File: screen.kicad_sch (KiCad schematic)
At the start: 12 parts, among them U4 3寸液晶屏TFT 全新无定义资料, U9 STI9287C

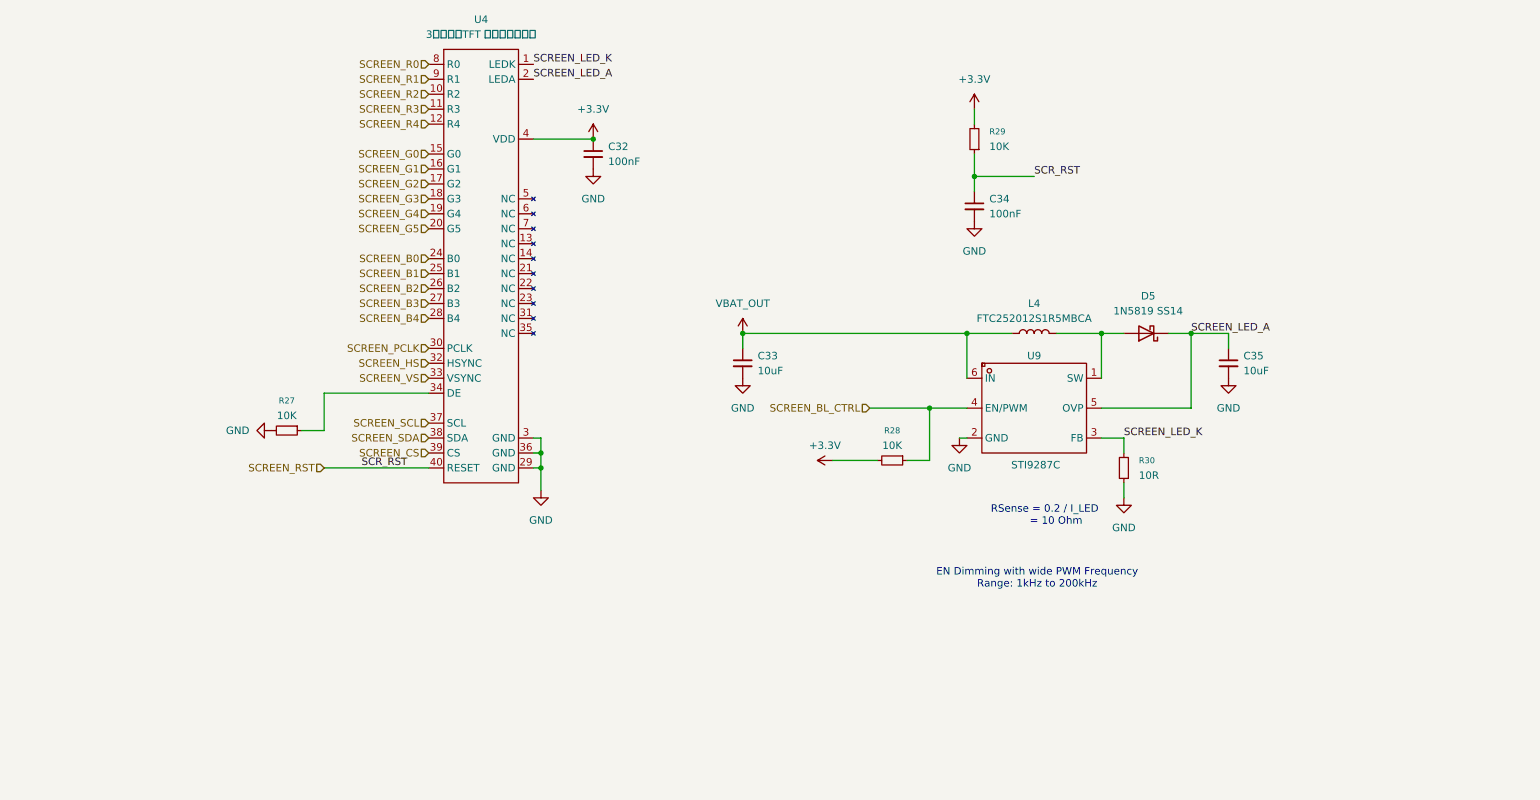
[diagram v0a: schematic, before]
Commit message: V0.3.1 bugfix
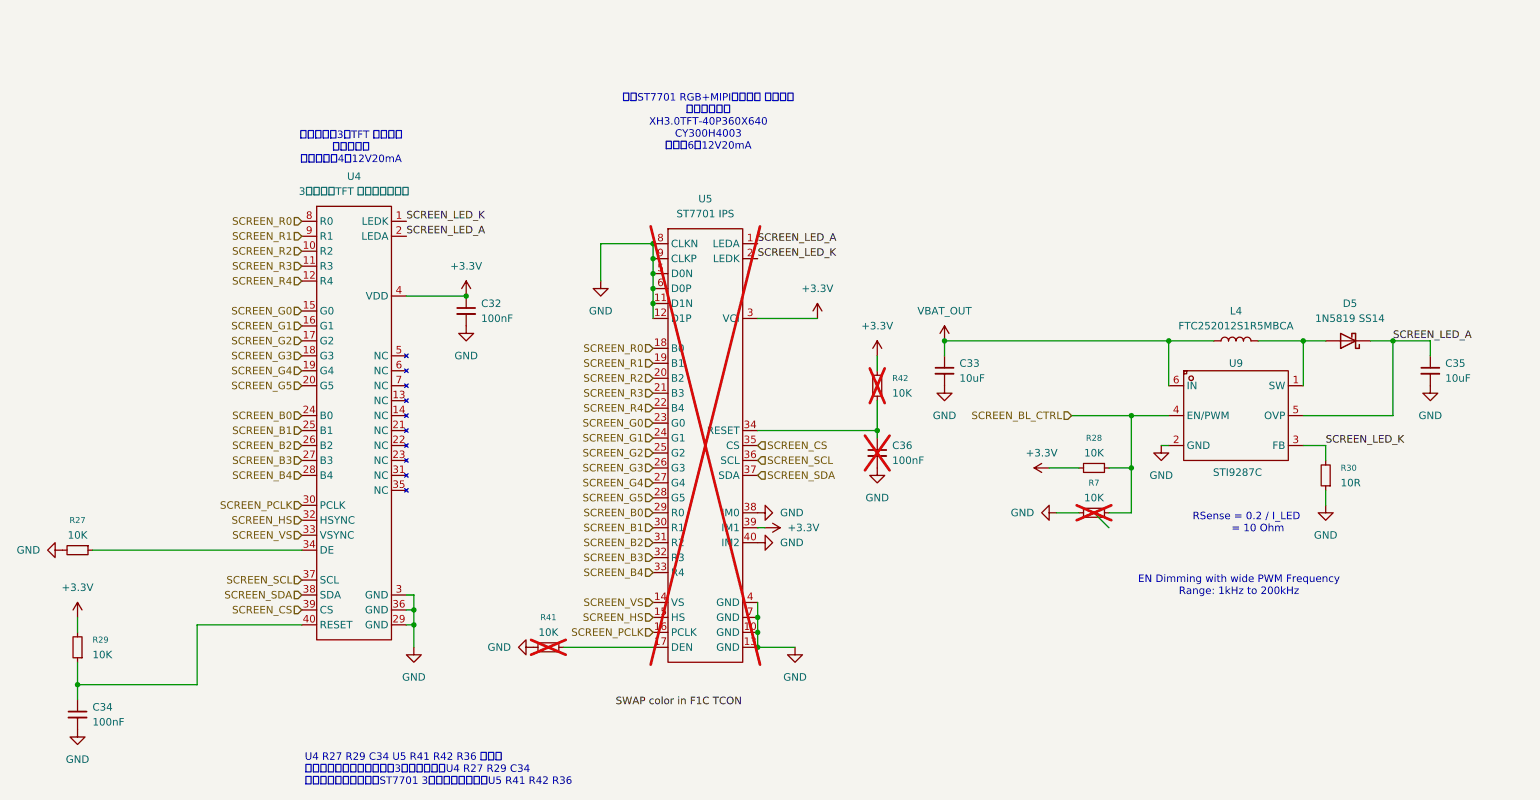
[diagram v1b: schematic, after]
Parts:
- added C36: 100nF, Capacitor_SMD:C_0603_1608Metric, symbol Device:C_Small
- added R41, R42, R7: 10K, Resistor_SMD:R_0603_1608Metric, symbol Device:R_Small
- added U5: ST7701 IPS, Connector_FFC-FPC:Hirose_FH12-40S-0.5SH_1x40-1MP_P0.50mm_Horizontal, symbol shirogane:CY300H4003
- C34, R27, R29, U4: 特殊说明 (none) -> 3元TFT贴装
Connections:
- net +3.3V: now also R42.2, U5.3 (VCI), U5.39 (IM1)
- net GND: now also C36.2, R41.2, R7.2, U5.10 (GND), U5.11 (D1N), U5.12 (D1P), U5.13 (GND), U5.38 (IM0), U5.4 (GND), U5.40 (IM2), U5.5 (D0N), U5.6 (D0P), U5.7 (GND), U5.8 (CLKN), U5.9 (CLKP)
- net SCREEN_B0: now also U5.29 (R0)
- net SCREEN_B1: now also U5.30 (R1)
- net SCREEN_B2: now also U5.31 (R2)
- net SCREEN_B3: now also U5.32 (R3)
- net SCREEN_B4: now also U5.33 (R4)
- net SCREEN_BL_CTRL: now also R7.1
- net SCREEN_CS: now also U5.35 (CS)
- net SCREEN_G0: now also U5.23 (G0)
- net SCREEN_G1: now also U5.24 (G1)
- net SCREEN_G2: now also U5.25 (G2)
- net SCREEN_G3: now also U5.26 (G3)
- net SCREEN_G4: now also U5.27 (G4)
- net SCREEN_G5: now also U5.28 (G5)
- net SCREEN_HS: now also U5.15 (HS)
- net SCREEN_LED_A: now also U5.1 (LEDA)
- net SCREEN_LED_K: now also U5.2 (LEDK)
- net SCREEN_PCLK: now also U5.16 (PCLK)
- net SCREEN_R0: now also U5.18 (B0)
- net SCREEN_R1: now also U5.19 (B1)
- net SCREEN_R2: now also U5.20 (B2)
- net SCREEN_R3: now also U5.21 (B3)
- net SCREEN_R4: now also U5.22 (B4)
- net SCREEN_SCL: now also U5.36 (SCL)
- net SCREEN_SDA: now also U5.37 (SDA)
- net SCREEN_VS: now also U5.14 (VS)
- net SCREEN_RST: no longer names the net of C34.1, R29.1, U4.40 (RESET)
- new net: R41.1, U5.17 (DEN)
- new net: C36.1, R42.1, U5.34 (RESET)
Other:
- note added: "U4 R27 R29 C34 U5 R41 R42 R36 说明： 若购买的屏幕是老王电子的3元屏，只贴装U4 R27 R29 C34 若购买的屏幕是通用的ST7701 3寸钢壳屏，只贴装U5 R41 R42 R36"
- note added: "老王电子的3元TFT 下接！！ （已断货） 此款背光为4串12V20mA"
- note added: "通用ST7701 RGB+MIPI屏幕接口 上接！！ 已测试型号： XH3.0TFT-40P360X640 CY300H4003 背光：6串12V20mA"
- moved on the sheet: C32, C33, C34, C35, D5, L4, R27, R28, R29, R30, U4, U9

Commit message: V0.5
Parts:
- C35: value 10uF -> 1uF
- D5: value 1N5819 SS14 -> 1N5819WS
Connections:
- net GND: now also U4.MP, U5.MP
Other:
- note added: "50V耐压！"
- note added: "SWAP color in F1C TCON"
- note added: "U4 R27 R29 C34 U5 R41 R42 R36 说明： 若购买的屏幕是老王电子的3元屏，只贴装U4 R27 R29 C34 若购买的屏幕是通用的ST7701 3寸钢壳屏，只贴装U5 R41 R42 C36"
- note removed: "U4 R27 R29 C34 U5 R41 R42 R36 说明： 若购买的屏幕是老王电子的3元屏，只贴装U4 R27 R29 C34 若购买的屏幕是通用的ST7701 3寸钢壳屏，只贴装U5 R41 R42 R36"
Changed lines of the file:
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@@
 		(comment 1 "V0.3 添加屏幕兼容接口，添加SD卡槽，优化布线")
 		(comment 2 "V0.3.1 BUG修复")
+		(comment 3 "土豆、星语Studio、爱莉希雅、所有复刻群友的支持！")
+		(comment 4 "V0.3.2 生产优化。特别感谢：（不分先后）和光、薄云、烟雨、WXNA、")
 	)
 	(text "RSense = 0.2 / I_LED \n       = 10 Ohm"
@@
 		)
 	)
-	(text "U4 R27 R29 C34 U5 R41 R42 R36 说明：\n若购买的屏幕是老王电子的3元屏，只贴装U4 R27 R29 C34\n若购买的屏幕是通用的ST7701 3寸钢壳屏，只贴装U5 R41 R42 R36"
+	(text "50V耐压！"
+		(exclude_from_sim no)
+		(at 269.24 102.616 0)
+		(effects
+			(font
+				(size 1.27 1.27)
+			)
+		)
+	)
+	(text "SWAP color in F1C TCON"
+		(exclude_from_sim no)
+		(at 135.636 159.004 0)
+		(effects
+			(font
+				(size 1.27 1.27)
+			)
+		)
+	)
+	(text "U4 R27 R29 C34 U5 R41 R42 R36 说明：\n若购买的屏幕是老王电子的3元屏，只贴装U4 R27 R29 C34\n若购买的屏幕是通用的ST7701 3寸钢壳屏，只贴装U5 R41 R42 C36"
 		(exclude_from_sim no)
 		(at 66.548 170.688 0)
@@
 	)
 	(junction
+		(at 143.51 142.24)
+		(diameter 0)
+		(color 0 0 0 0)
+	)
+	(junction
 		(at 125.73 86.36)
 		(diameter 0)
@@
 	)
 	(junction
+		(at 85.09 140.97)
+		(diameter 0)
+		(color 0 0 0 0)
+	)
+	(junction
 		(at 125.73 83.82)
 		(diameter 0)
@@
 		(color 0 0 0 0)
 	)
-	(bus_entry
-		(at 200.66 127)
-		(size 2.54 2.54)
-		(stroke
-			(width 0)
-			(type default)
-		)
-	)
 	(wire
 		(pts
@@
 	(wire
 		(pts
+			(xy 85.09 138.43) (xy 85.09 140.97)
+		)
+		(stroke
+			(width 0)
+			(type default)
+		)
+	)
+	(wire
+		(pts
 			(xy 116.84 81.28) (xy 125.73 81.28)
 		)
@@
 	(wire
 		(pts
+			(xy 143.51 139.7) (xy 143.51 142.24)
+		)
+		(stroke
+			(width 0)
+			(type default)
+		)
+	)
+	(wire
+		(pts
 			(xy 207.01 127) (xy 207.01 119.38)
 		)
@@
 		(pts
 			(xy 30.48 133.35) (xy 66.04 133.35)
+		)
+		(stroke
+			(width 0)
+			(type default)
+		)
+	)
+	(wire
+		(pts
+			(xy 83.82 138.43) (xy 85.09 138.43)
 		)
 		(stroke
@@
 	(label "SCREEN_LED_A"
 		(at 83.82 80.01 0)
-		(effects
-			(font
-				(size 1.27 1.27)
-			)
-			(justify left bottom)
-		)
-	)
-	(label "SWAP color in F1C TCON"
-		(at 119.38 160.02 0)
 		(effects
 			(font
@@
 		(pin "29"
 		)
+		(pin "MP"
+		)
 		(instances
 			(project ""
@@
 			)
 		)
-		(property "Value" "10uF"
+		(property "Value" "1uF"
 			(at 260.35 104.1462 0)
 			(effects
@@
 		(pin "36"
 		)
+		(pin "MP"
+		)
 		(instances
 			(project ""
@@
 			)
 		)
-		(property "Value" "1N5819 SS14"
+		(property "Value" "1N5819WS"
 			(at 244.1575 93.98 0)
 			(effects
